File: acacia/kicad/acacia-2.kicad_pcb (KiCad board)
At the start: 2 copper layers, 268 x 112 mm, 124 parts, among them J1 GroveMiniTrack, J2 TM040040, J3 USB4105-GF-A-060, SW1 Q, SW10 P, SW11 A, SW12 S, SW13 D, SW14 F, SW15 G, SW16 H, SW17 J, SW18 K, SW19 L, SW2 W, SW20 B, SW21 RESET, SW22 Z, SW23 X, SW24 C, SW25 V, SW26 Sft, SW27 Spc, SW28 N, SW29 M, SW3 E, SW30 Com, SW31 Dot, SW32 Tab, SW33 Prv, SW34 L1, SW35 AGr, SW36 Esc, SW37 Del, SW38 Nxt, SW39 Ent, SW4 R, SW5 T, SW6 Y, SW7 U, SW8 I, SW9 O, U1 ATmega32U4-A, U2 USBLC6-2SC6, Y1 16MHz

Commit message: V2 gerber
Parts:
- D39, D40, D41, D42, D43, D44: footprint LED_SMD:LED_SK6805_PLCC4_2.4x2.7mm_P1.3mm -> LED_SMD:LED_SK6812_EC15_1.5x1.5mm
- J1: moved to B.Cu
- moved TP2 2.25 mm to (165.0, 70.8)
- moved TP1 1.25 mm to (165.0, 66.8)
- moved J1 1.00 mm to (139.5, 98.0)
- moved C6 0.57 mm to (141.0, 110.0)
- turned D39 to 165 degrees
- turned D40 to 165 degrees
- turned D41 to 165 degrees
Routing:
- net +5V: track 276.6 -> 297.0 mm, vias 8 -> 6
- net GNDD: track 185.9 -> 169.2 mm, vias 12 -> 13
- net Net-(D39-DOUT): track 29.4 -> 25.6 mm
- net Net-(D40-DOUT): track 24.4 -> 21.0 mm
- net Net-(D41-DOUT): track 24.9 -> 22.5 mm
- net RGB: track 77.5 -> 75.9 mm
- net C3: track 113.6 -> 113.0 mm
- net /SDA: track 29.2 -> 29.6 mm, vias 0 -> 1
- net /SCL: track 28.5 -> 28.3 mm, vias 0 -> 1
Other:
- outline, holes or cut-outs redrawn

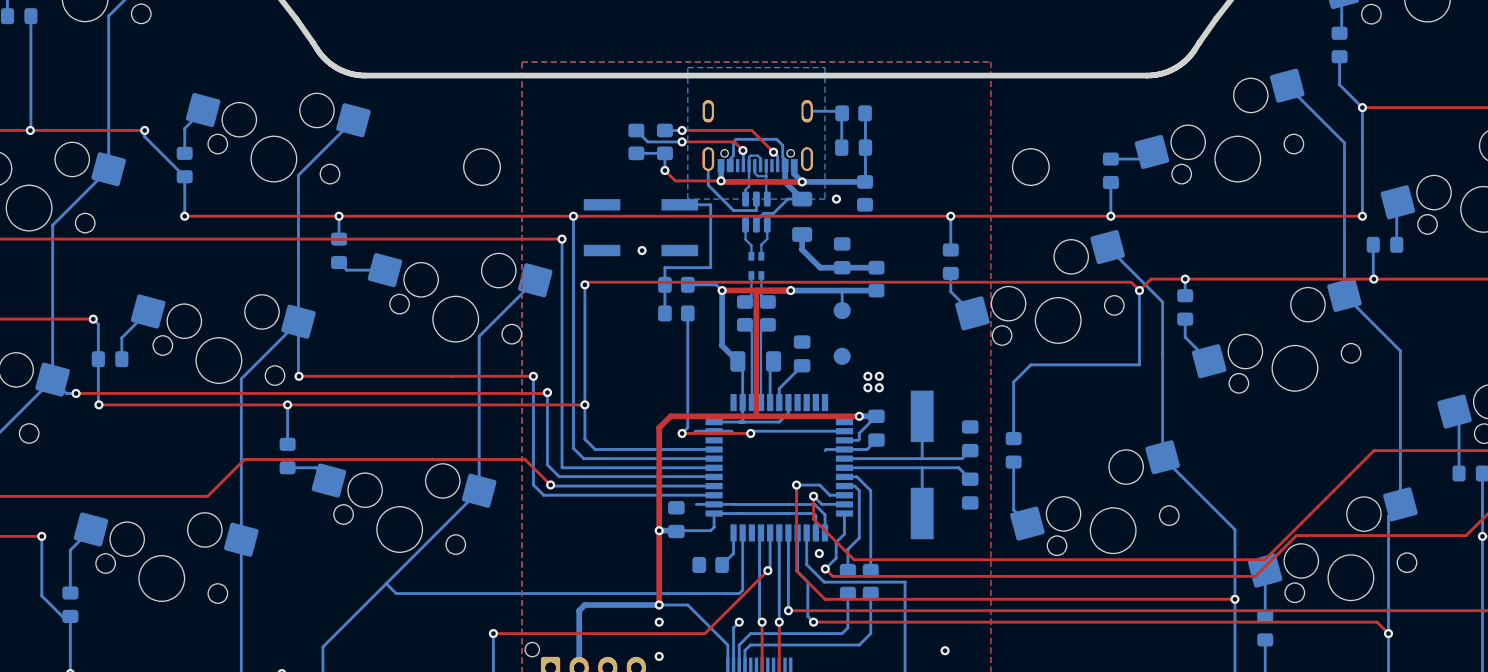
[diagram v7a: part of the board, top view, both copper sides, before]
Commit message: Adjust key position to better fit actual layout
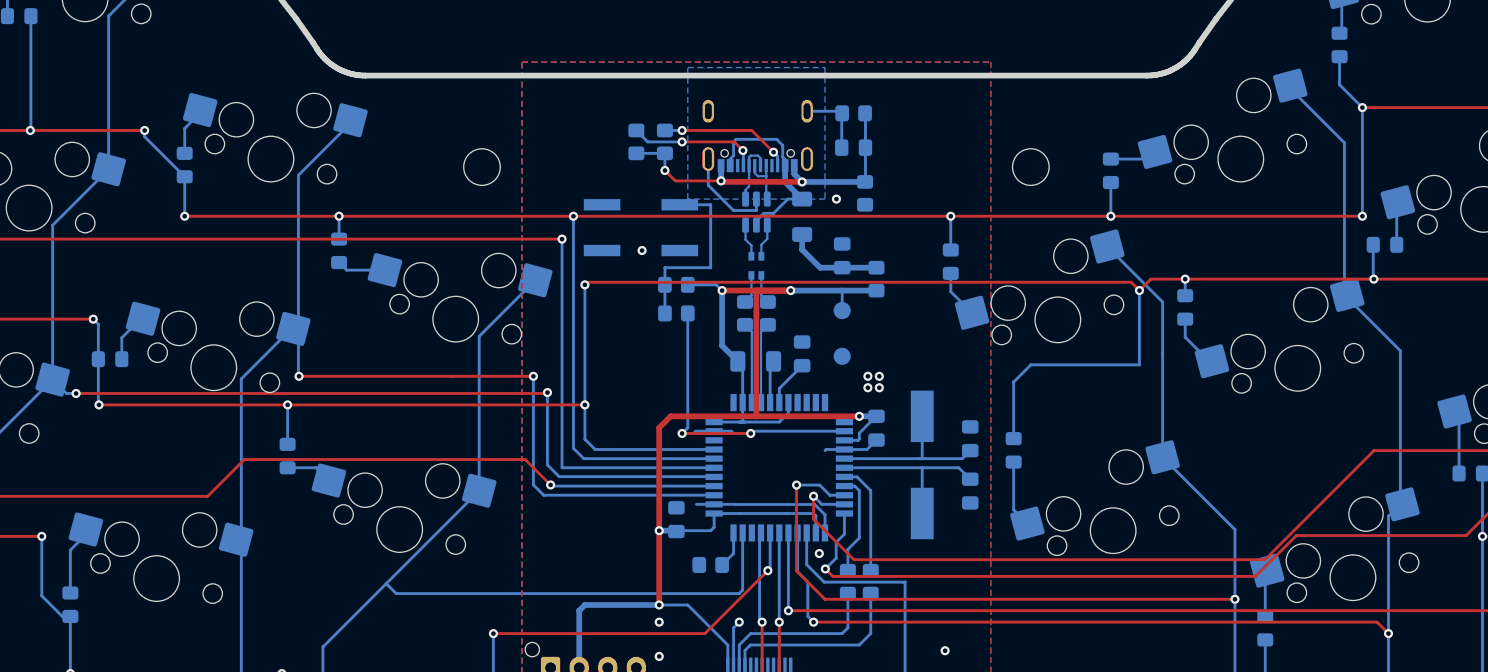
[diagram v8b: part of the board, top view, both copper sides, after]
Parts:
- moved SW14 0.77 mm to (110.0, 71.7)
- moved SW25 0.45 mm to (105.0, 90.2)
- moved SW7 0.26 mm to (199.9, 53.5)
- moved SW4 0.26 mm to (115.0, 53.5)
- moved SW17 0.24 mm to (204.8, 71.8)
- moved SW28 0.18 mm to (209.7, 90.1)
- moved SW6 0.06 mm to (183.9, 67.6)
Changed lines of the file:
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@@
   )
   (footprint "mech-kbd:MX-Hotswap-1U" locked (layer "F.Cu")
-    (at 209.493097 90.114801 15)
+    (at 209.671862 90.114801 15)
     (property "Sheetfile" "acacia-2.kicad_sch")
     (property "Sheetname" "")
@@
   )
   (footprint "mech-kbd:MX-Hotswap-1U" locked (layer "F.Cu")
-    (at 105.493097 90.185199 -15)
+    (at 105.042261 90.185199 -15)
     (property "Sheetfile" "acacia-2.kicad_sch")
     (property "Sheetname" "")
@@
   )
   (footprint "mech-kbd:MX-Hotswap-1U" locked (layer "F.Cu")
-    (at 199.6 53.5 15)
+    (at 199.861349 53.5 15)
     (property "Sheetfile" "acacia-2.kicad_sch")
     (property "Sheetname" "")
@@
   )
   (footprint "mech-kbd:MX-Hotswap-1U" locked (layer "F.Cu")
-    (at 115.3 53.5 -15)
+    (at 115.042261 53.5 -15)
     (property "Sheetfile" "acacia-2.kicad_sch")
     (property "Sheetname" "")
@@
   )
   (footprint "mech-kbd:MX-Hotswap-1U" locked (layer "F.Cu")
-    (at 183.893097 67.614801 15)
+    (at 183.861349 67.564304 15)
     (property "Sheetfile" "acacia-2.kicad_sch")
     (property "Sheetname" "")
@@
   )
   (footprint "mech-kbd:MX-Hotswap-1U" locked (layer "F.Cu")
-    (at 204.6 71.8 15)
+    (at 204.843097 71.8 15)
     (property "Sheetfile" "acacia-2.kicad_sch")
     (property "Sheetname" "")
@@
     )
   )
-  (footprint "mech-kbd:MX-Hotswap-1U" (layer "F.Cu")
-    (at 110.49 71.12 -15)
+  (footprint "mech-kbd:MX-Hotswap-1U" locked (layer "F.Cu")
+    (at 110.042261 71.749503 -15)
     (property "Sheetfile" "acacia-2.kicad_sch")
     (property "Sheetname" "")
@@
     (fp_arc (start -2.4 -0.6) (mid -1.814214 -2.014214) (end -0.4 -2.6)
       (stroke (width 0.127) (type solid)) (layer "B.CrtYd"))
-    (pad "" np_thru_hole circle (at -5.08 0 33.099) (size 1.7018 1.7018) (drill 1.7018) (layers "F&B.Cu" "*.Mask"))
-    (pad "" np_thru_hole circle (at -3.81 -2.54 345) (size 3 3) (drill 3) (layers "F&B.Cu" "*.Mask"))
-    (pad "" np_thru_hole circle (at 0 0 345) (size 3.9878 3.9878) (drill 3.9878) (layers "F&B.Cu" "*.Mask"))
-    (pad "" np_thru_hole circle (at 2.54 -5.08 345) (size 3 3) (drill 3) (layers "F&B.Cu" "*.Mask"))
-    (pad "" np_thru_hole circle (at 5.08 0 33.099) (size 1.7018 1.7018) (drill 1.7018) (layers "F&B.Cu" "*.Mask"))
-    (pad "1" smd roundrect (at -7.085 -2.54 345) (size 2.55 2.5) (layers "B.Cu" "B.Paste" "B.Mask") (roundrect_rratio 0.08)
+    (pad "" np_thru_hole circle locked (at -5.08 0 33.099) (size 1.7018 1.7018) (drill 1.7018) (layers "F&B.Cu" "*.Mask"))
+    (pad "" np_thru_hole circle locked (at -3.81 -2.54 345) (size 3 3) (drill 3) (layers "F&B.Cu" "*.Mask"))
+    (pad "" np_thru_hole circle locked (at 0 0 345) (size 3.9878 3.9878) (drill 3.9878) (layers "F&B.Cu" "*.Mask"))
+    (pad "" np_thru_hole circle locked (at 2.54 -5.08 345) (size 3 3) (drill 3) (layers "F&B.Cu" "*.Mask"))
+    (pad "" np_thru_hole circle locked (at 5.08 0 33.099) (size 1.7018 1.7018) (drill 1.7018) (layers "F&B.Cu" "*.Mask"))
+    (pad "1" smd roundrect locked (at -7.085 -2.54 345) (size 2.55 2.5) (layers "B.Cu" "B.Paste" "B.Mask") (roundrect_rratio 0.08)
       (net 24 "Net-(D14-A)") (pinfunction "1") (pintype "passive"))
-    (pad "2" smd roundrect (at 5.842 -5.08 345) (size 2.55 2.5) (layers "B.Cu" "B.Paste" "B.Mask") (roundrect_rratio 0.08)
+    (pad "2" smd roundrect locked (at 5.842 -5.08 345) (size 2.55 2.5) (layers "B.Cu" "B.Paste" "B.Mask") (roundrect_rratio 0.08)
       (net 75 "C3") (pinfunction "2") (pintype "passive"))
   )
